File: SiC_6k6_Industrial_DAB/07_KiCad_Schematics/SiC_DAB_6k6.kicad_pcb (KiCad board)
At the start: 6 copper layers, 340 x 250 mm, 259 parts, among them J1 HV+, J10 BoosterPack J1/J3, J11 BoosterPack J2/J4, J12 BoosterPack PWM, J13 +24V IN, J14 CAN, J15 UART, J16 RELAY/FAN, J17 INTERLOCK IN, J18 NTC1, J19 NTC2, J2 HV-, J20 PE, J3 SW_A, J4 SW_B, J5 LV+, J6 LV-, J7 SW_C, J8 SW_D, J9 L1 (via CT), Q1 C3M0032120K, Q2 C3M0032120K, Q3 C3M0032120K, Q4 C3M0032120K, Q5 C3M0016120K, Q6 C3M0016120K, Q7 C3M0016120K, Q8 C3M0016120K, U1 UCC21520DW, U10 LM393, U11 LM393, U12 74HC32, U13 TSR 3-24120, U14 TSR 1-2450, U15 AMS1117-3.3, U16 TCAN332, U17 ULN2003A, U18 PC817, U19 PC817, U2 UCC21520DW, U3 UCC21520DW, U4 UCC21520DW, U5 AMC1301, U6 AMC1301, U7 AMC1301, U8 TLV9062, U9 TLV9062

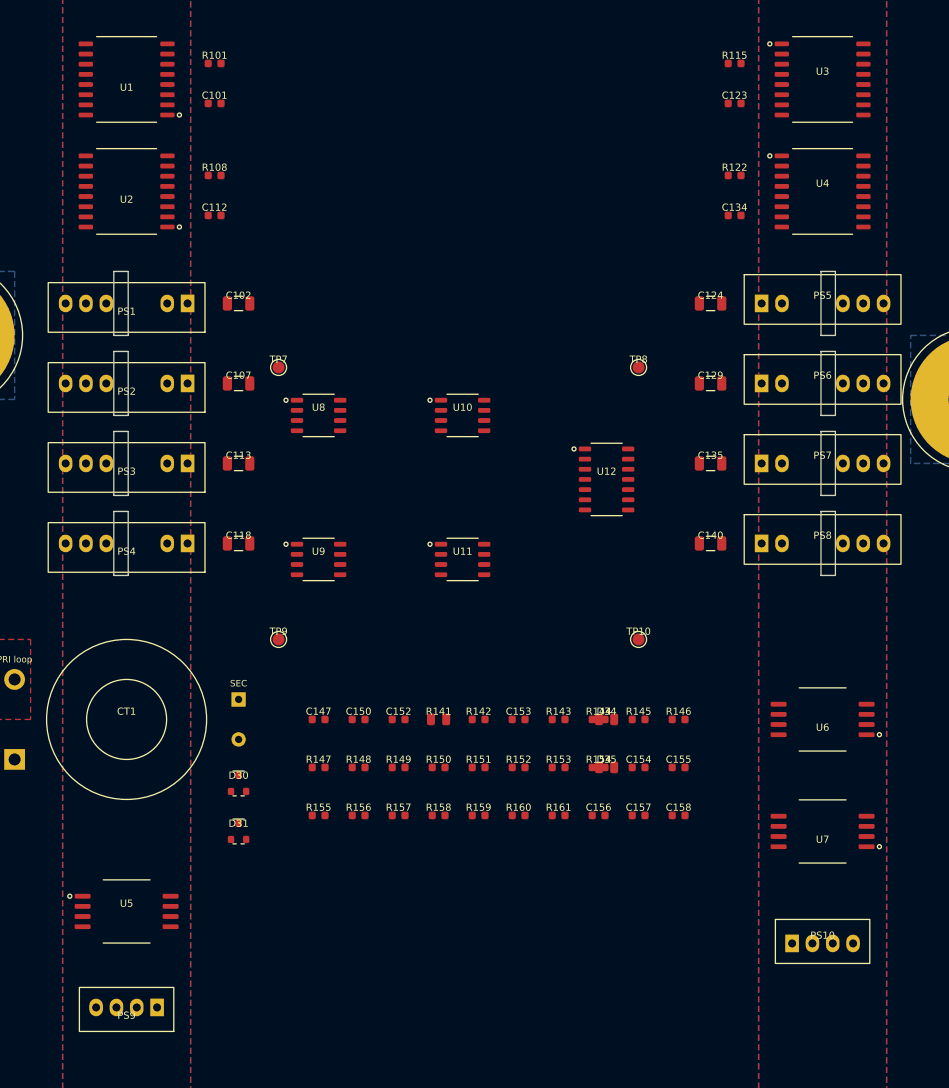
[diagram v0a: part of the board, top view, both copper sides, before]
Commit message: Router hard pass with rip-up retry, exact halo radii, via cost dilation; DAB: driver passives off the fan-out corridors, PS9/PS10 SIP-7 1 W module footprint, 0.5 mm control-power tracks; PSFB: DT resistor/TP placement
- NegotiatedRouter: full/small halo masks give the exact d < hw_a+hw_b+clearance
  overlap test; A* via placement sees the via halo; nets still in conflict after
  the negotiation are re-routed against hard obstacles, with a bounded rip-up
  retry, so emitted copper never violates the clearance model.
- Fan-out: plane-net vias 1.2 mm beyond the long stubs; corridors long+1.5 mm;
  unreachable terminals are reported.
- plot_board.py: matplotlib region renderer for layout review.
- DAB: PS9/PS10 changed from a 2.54 mm SIP-4 (cannot meet the 5.5 mm module
  creepage rule) to a SIP-7 outline 1 W module (part TBD, flagged in BOM and
  insulation table); DT resistors / VCCI caps moved clear of the driver
  fan-out corridors; private regions and slots for PS9/PS10.

Co-Authored-By: Claude Fable 5.1 <noreply@anthropic.com>
Claude-Session: https://claude.ai/code/session_01TJ4PYx4qhHYB2ApeFHUZoW
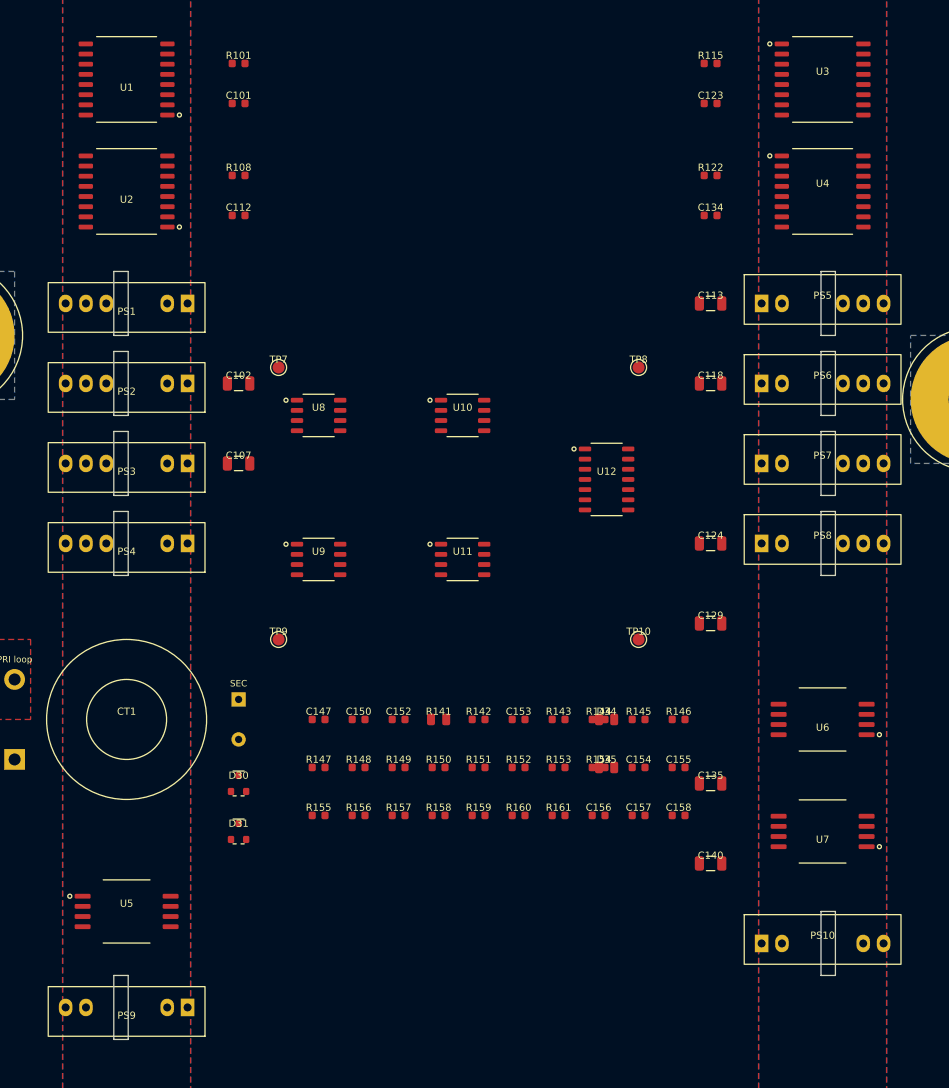
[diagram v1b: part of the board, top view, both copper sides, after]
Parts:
- PS10, PS9: value R1SE-0505 -> ISO 5V/5V 1W SIP-7; footprint SIP-4_IsoDCDC -> SIP-7_IsoDCDC_1W
- moved C113 62.3 mm to (199.0, 48.0)
- moved C118 62.3 mm to (199.0, 58.0)
- moved C135 40.0 mm to (199.0, 108.0)
- moved C140 40.0 mm to (199.0, 118.0)
- moved C124 30.0 mm to (199.0, 78.0)
- moved C129 30.0 mm to (199.0, 88.0)
- moved C102 10.0 mm to (140.0, 58.0)
- moved C107 10.0 mm to (140.0, 68.0)
- moved C101 3.00 mm to (140.0, 23.0)
- moved C112 3.00 mm to (140.0, 37.0)
- moved C123 3.00 mm to (199.0, 23.0)
- moved C134 3.00 mm to (199.0, 37.0)
- moved R101 3.00 mm to (140.0, 18.0)
- moved R108 3.00 mm to (140.0, 32.0)
- moved R115 3.00 mm to (199.0, 18.0)
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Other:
- outline, holes or cut-outs redrawn

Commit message: Router: recursive rip-up retry with state snapshots, same-net task merge; DAB: per-region PE lugs with PE clearance class, net-class fixes (SW_A_CT, SH_N, SH_NS), placement fixes (U15, U18/U19, TP1, bias caps); tools/kicad README
Co-Authored-By: Claude Fable 5.1 <noreply@anthropic.com>
Claude-Session: https://claude.ai/code/session_01TJ4PYx4qhHYB2ApeFHUZoW
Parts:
- added J21: PE_HV, Lug_M5, F.Cu at (42.0, 236.0)
- added J22: PE_LV, Lug_M5, F.Cu at (270.0, 236.0)
- moved C113 64.2 mm to (138.0, 68.0)
- moved C118 64.2 mm to (138.0, 78.0)
- moved C124 20.0 mm to (199.0, 58.0)
- moved C129 20.0 mm to (199.0, 68.0)
- moved C135 20.0 mm to (199.0, 88.0)
- moved C140 20.0 mm to (199.0, 98.0)
- moved C102 10.2 mm to (138.0, 48.0)
- moved C107 10.2 mm to (138.0, 58.0)
- moved TP1 8.94 mm to (96.0, 110.0)
- moved U18 7.00 mm to (150.0, 181.0)
- moved U19 7.00 mm to (162.0, 181.0)
- moved U15 6.00 mm to (182.0, 212.0)
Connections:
- CY1 pad 2: PE -> PE_HV
- CY2 pad 2: PE -> PE_HV
- CY3 pad 2: PE -> PE_LV
- CY4 pad 2: PE -> PE_LV

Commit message: DAB board: intermediate generated board, DRC report and manufacturing outputs (final routing run in progress)
Co-Authored-By: Claude Fable 5.1 <noreply@anthropic.com>
Claude-Session: https://claude.ai/code/session_01TJ4PYx4qhHYB2ApeFHUZoW
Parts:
- C1, C2, C3, C4: footprint C_Film_P52.5 -> SiC_DAB:C_Film_P52.5
- C10, C11, C12, C9: footprint C_Film_P37.5 -> SiC_DAB:C_Film_P37.5
- C101, C104, C106, C109, C111, C112, C115, C117, C120, C122, C123, C126, C128, C131, C133, C134, C137, C139, C142, C144, C145, C146, C147, C148, C149, C150, C151, C152, C153, C154, C155, C156, C157, C158, C165, C166: footprint C_0603 -> SiC_DAB:C_0603
- C102, C103, C107, C108, C113, C114, C118, C119, C124, C125, C129, C130, C135, C136, C140, C141, C161, C163, C164: footprint C_1206 -> SiC_DAB:C_1206
- C105, C110, C116, C121, C127, C132, C138, C143: footprint C_0805 -> SiC_DAB:C_0805
- C13, C14, C15, C16, C5, C6, C7, C8: footprint C_2220 -> SiC_DAB:C_2220
- C159, C160, C162: footprint C_Radial_D8_P3.5 -> SiC_DAB:C_Radial_D8_P3.5
- CT1: footprint CT_Toroid_Straddle -> SiC_DAB:CT_Toroid_Straddle
- CY1, CY2, CY3, CY4: footprint C_Y1_P12.5 -> SiC_DAB:C_Y1_P12.5
- D21, D22, D23, D24, D25, D26, D27, D28, D32, D33: footprint D_SMA -> SiC_DAB:D_SMA
- D30, D31: footprint SOT-23 -> SiC_DAB:SOT-23
- D34, D35: footprint LED_0805 -> SiC_DAB:LED_0805
- F1, F2: footprint Fuse_Terminal_M6 -> SiC_DAB:Fuse_Terminal_M6
- H1, H2, H3, H4, H5, H6: footprint MountingHole_M4 -> SiC_DAB:MountingHole_M4
- J1, J2, J3, J4, J5, J6, J7, J8, J9: footprint Stud_M6 -> SiC_DAB:Stud_M6
- J10, J11: footprint PinHeader_2x10_P2.54 -> SiC_DAB:PinHeader_2x10_P2.54
- J12, J16, J17: footprint PinHeader_1x08_P2.54 -> SiC_DAB:PinHeader_1x08_P2.54
- J13, J14: footprint TerminalBlock_1x02_P5.08 -> SiC_DAB:TerminalBlock_1x02_P5.08
- J15, J18, J19: footprint PinHeader_1x02_P2.54 -> SiC_DAB:PinHeader_1x02_P2.54
- J20, J21, J22: footprint Lug_M5 -> SiC_DAB:Lug_M5
- PS1, PS2, PS3, PS4, PS5, PS6, PS7, PS8: footprint SIP-7_IsoDCDC -> SiC_DAB:SIP-7_IsoDCDC
- PS10, PS9: footprint SIP-7_IsoDCDC_1W -> SiC_DAB:SIP-7_IsoDCDC_1W
- Q1, Q2, Q3, Q4, Q5, Q6, Q7, Q8: footprint TO-247-4_Vertical -> SiC_DAB:TO-247-4_Vertical
- R1, R2, R3, R4, R5, R6: footprint R_2512 -> SiC_DAB:R_2512
- R101, R104, R107, R108, R111, R114, R115, R118, R121, R122, R125, R128, R131, R132, R136, R137, R139, R140, R142, R143, R144, R145, R146, R147, R148, R149, R150, R151, R152, R153, R154, R155, R156, R157, R158, R159, R160, R161, R162, R163, R164, R165, R166, R168, R170, R171, R172: footprint R_0603 -> SiC_DAB:R_0603
- R102, R103, R105, R106, R109, R110, R112, R113, R116, R117, R119, R120, R123, R124, R126, R127, R129, R130, R134, R135, R173: footprint R_1206 -> SiC_DAB:R_1206
- R133, R138, R141, R167, R169: footprint R_0805 -> SiC_DAB:R_0805
- R7: footprint R_Shunt_8518 -> SiC_DAB:R_Shunt_8518
- TP1, TP10, TP11, TP12, TP13, TP2, TP3, TP4, TP5, TP6, TP7, TP8, TP9: footprint TestPoint -> SiC_DAB:TestPoint
- U1, U2, U3, U4: footprint SOIC-16W -> SiC_DAB:SOIC-16W
- U10, U11, U16, U8, U9: footprint SOIC-8 -> SiC_DAB:SOIC-8
- U12: footprint SOIC-14 -> SiC_DAB:SOIC-14
- U13, U14: footprint SIP-3_TSR -> SiC_DAB:SIP-3_TSR
- U15: footprint SOT-223 -> SiC_DAB:SOT-223
- U17: footprint SOIC-16 -> SiC_DAB:SOIC-16
- U18, U19: footprint DIP-4 -> SiC_DAB:DIP-4
- U5, U6, U7: footprint SOIC-8W -> SiC_DAB:SOIC-8W
- moved J21 114.5 mm to (14.0, 125.0)
- moved C159 106.1 mm to (152.0, 90.0)
- moved C162 106.0 mm to (170.0, 90.0)
- moved C160 106.0 mm to (161.0, 90.0)
- moved C135 60.0 mm to (139.0, 88.0)
- moved C140 60.0 mm to (139.0, 98.0)
- moved D34 50.2 mm to (140.0, 120.0)
- moved D35 50.2 mm to (140.0, 126.0)
- moved C166 35.5 mm to (181.0, 196.0)
- moved R165 35.5 mm to (186.0, 196.0)
- moved R166 35.5 mm to (191.0, 196.0)
- moved C163 15.0 mm to (161.0, 196.0)
- moved C164 15.0 mm to (166.0, 196.0)
- moved C165 15.0 mm to (171.0, 196.0)
- moved R164 15.0 mm to (176.0, 196.0)
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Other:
- outline, holes or cut-outs redrawn

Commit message: DAB board: intermediate generated board and DRC report (run 17: 29 errors, routing run 19 in progress)
Co-Authored-By: Claude Fable 5.1 <noreply@anthropic.com>
Claude-Session: https://claude.ai/code/session_01TJ4PYx4qhHYB2ApeFHUZoW
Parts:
- moved TP6 23.9 mm to (232.0, 80.0)
- moved J20 12.0 mm to (152.0, 242.0)
- moved C135 11.7 mm to (145.0, 98.0)
- moved J3 8.00 mm to (92.0, 105.0)
- moved TP1 8.00 mm to (96.0, 118.0)
- moved TP10 6.08 mm to (199.0, 84.0)
- moved C140 6.00 mm to (145.0, 98.0)
- moved D30 6.00 mm to (146.0, 108.0)
- moved D31 6.00 mm to (146.0, 114.0)
- moved J7 4.00 mm to (236.0, 60.0)
- moved TP3 4.00 mm to (30.0, 56.0)
- moved U17 4.00 mm to (176.0, 186.0)
- moved C159 2.00 mm to (150.0, 90.0)
- moved C160 1.00 mm to (160.0, 90.0)

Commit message: DAB board: intermediate generated board and DRC report (run 19: 18 errors; run 20 in progress)
Co-Authored-By: Claude Fable 5.1 <noreply@anthropic.com>
Claude-Session: https://claude.ai/code/session_01TJ4PYx4qhHYB2ApeFHUZoW
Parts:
- moved J3 32.0 mm to (93.0, 73.0)
- moved TP1 32.0 mm to (96.0, 86.0)
- moved TP9 6.32 mm to (143.0, 84.0)
- moved C140 6.00 mm to (145.0, 104.0)
- moved C13 4.00 mm to (248.0, 38.0)
- moved C14 4.00 mm to (266.0, 38.0)
- moved C15 4.00 mm to (294.0, 38.0)
- moved C16 4.00 mm to (312.0, 38.0)
- moved C8 4.00 mm to (96.0, 38.0)
- moved J20 2.00 mm to (150.0, 242.0)

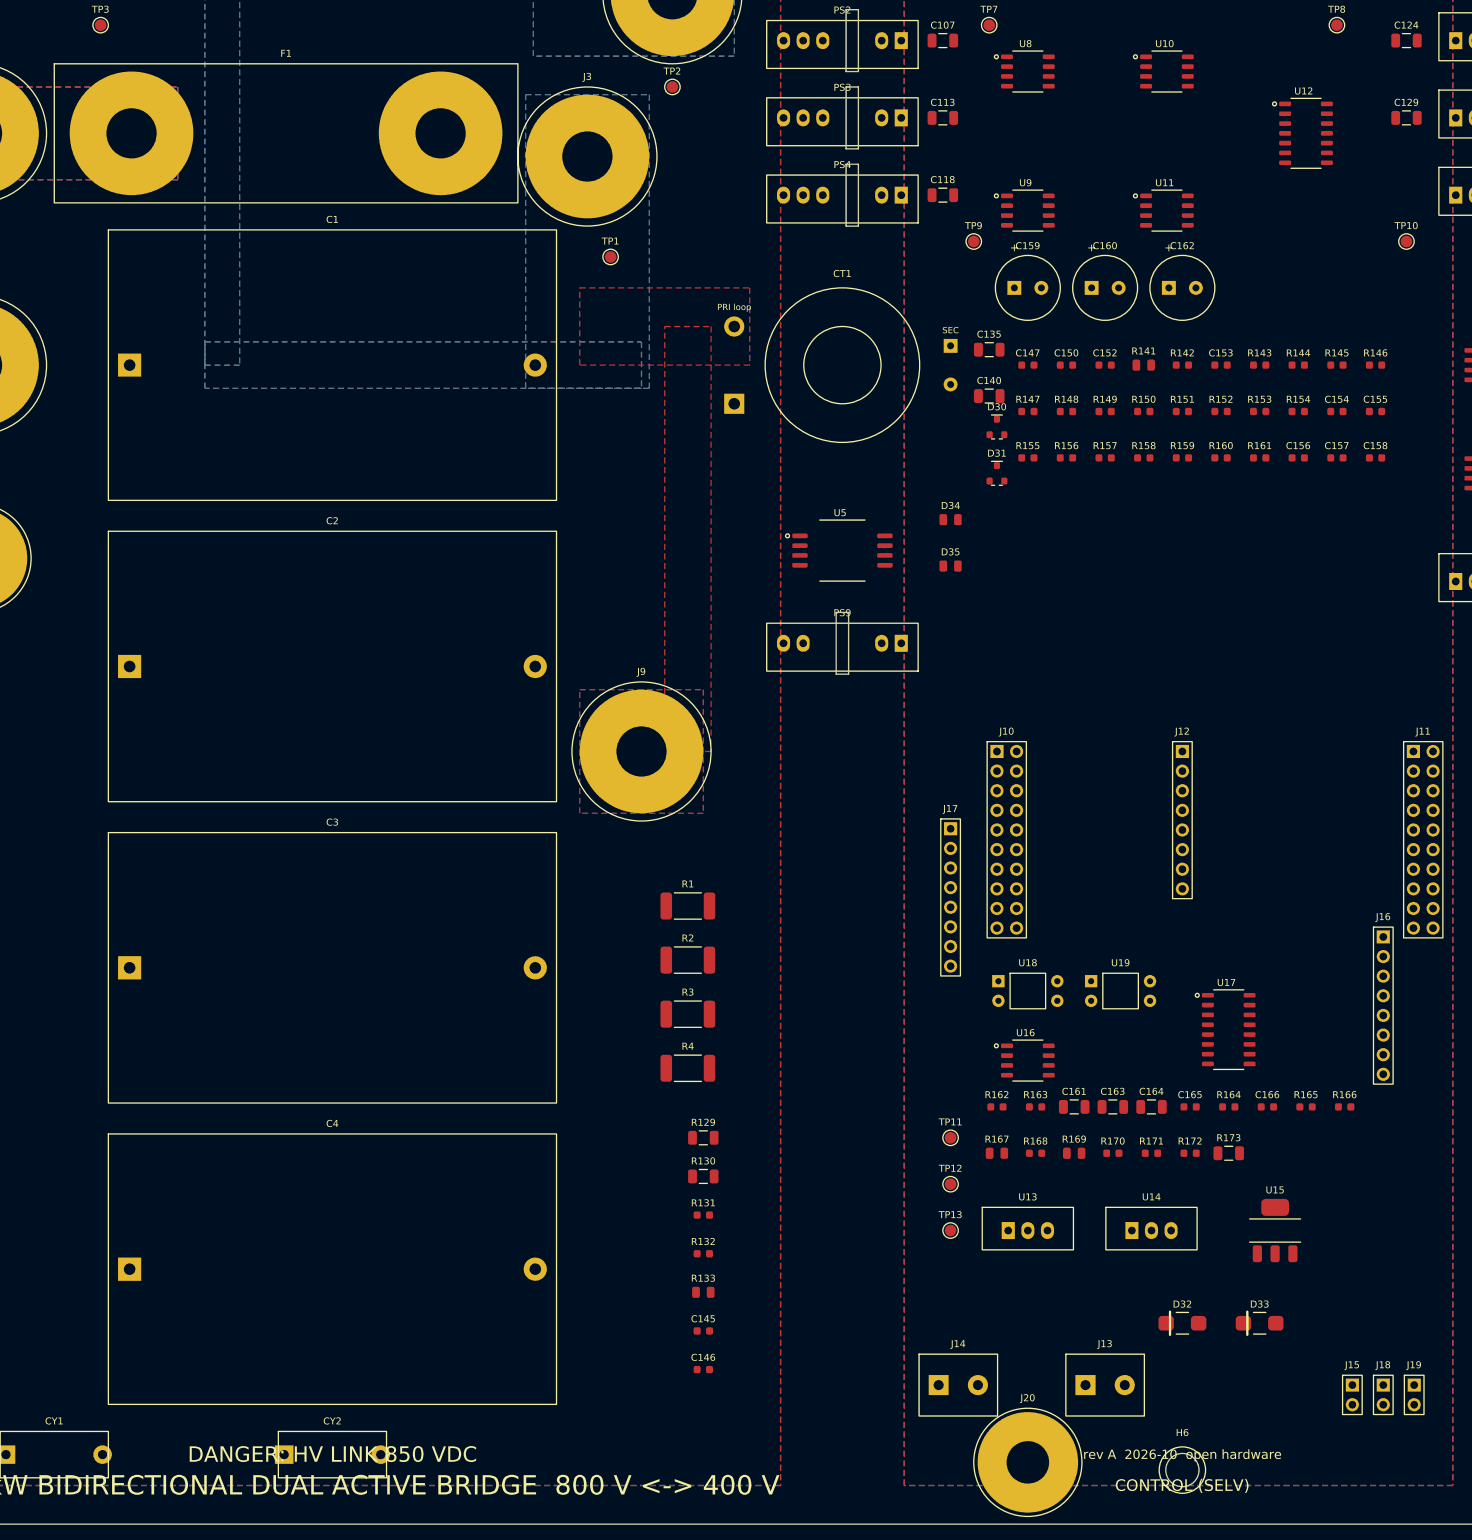
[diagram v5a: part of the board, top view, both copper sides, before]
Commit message: DAB board: intermediate generated board and DRC report (run 20: 6 errors; run 21 in progress)
Co-Authored-By: Claude Fable 5.1 <noreply@anthropic.com>
Claude-Session: https://claude.ai/code/session_01TJ4PYx4qhHYB2ApeFHUZoW
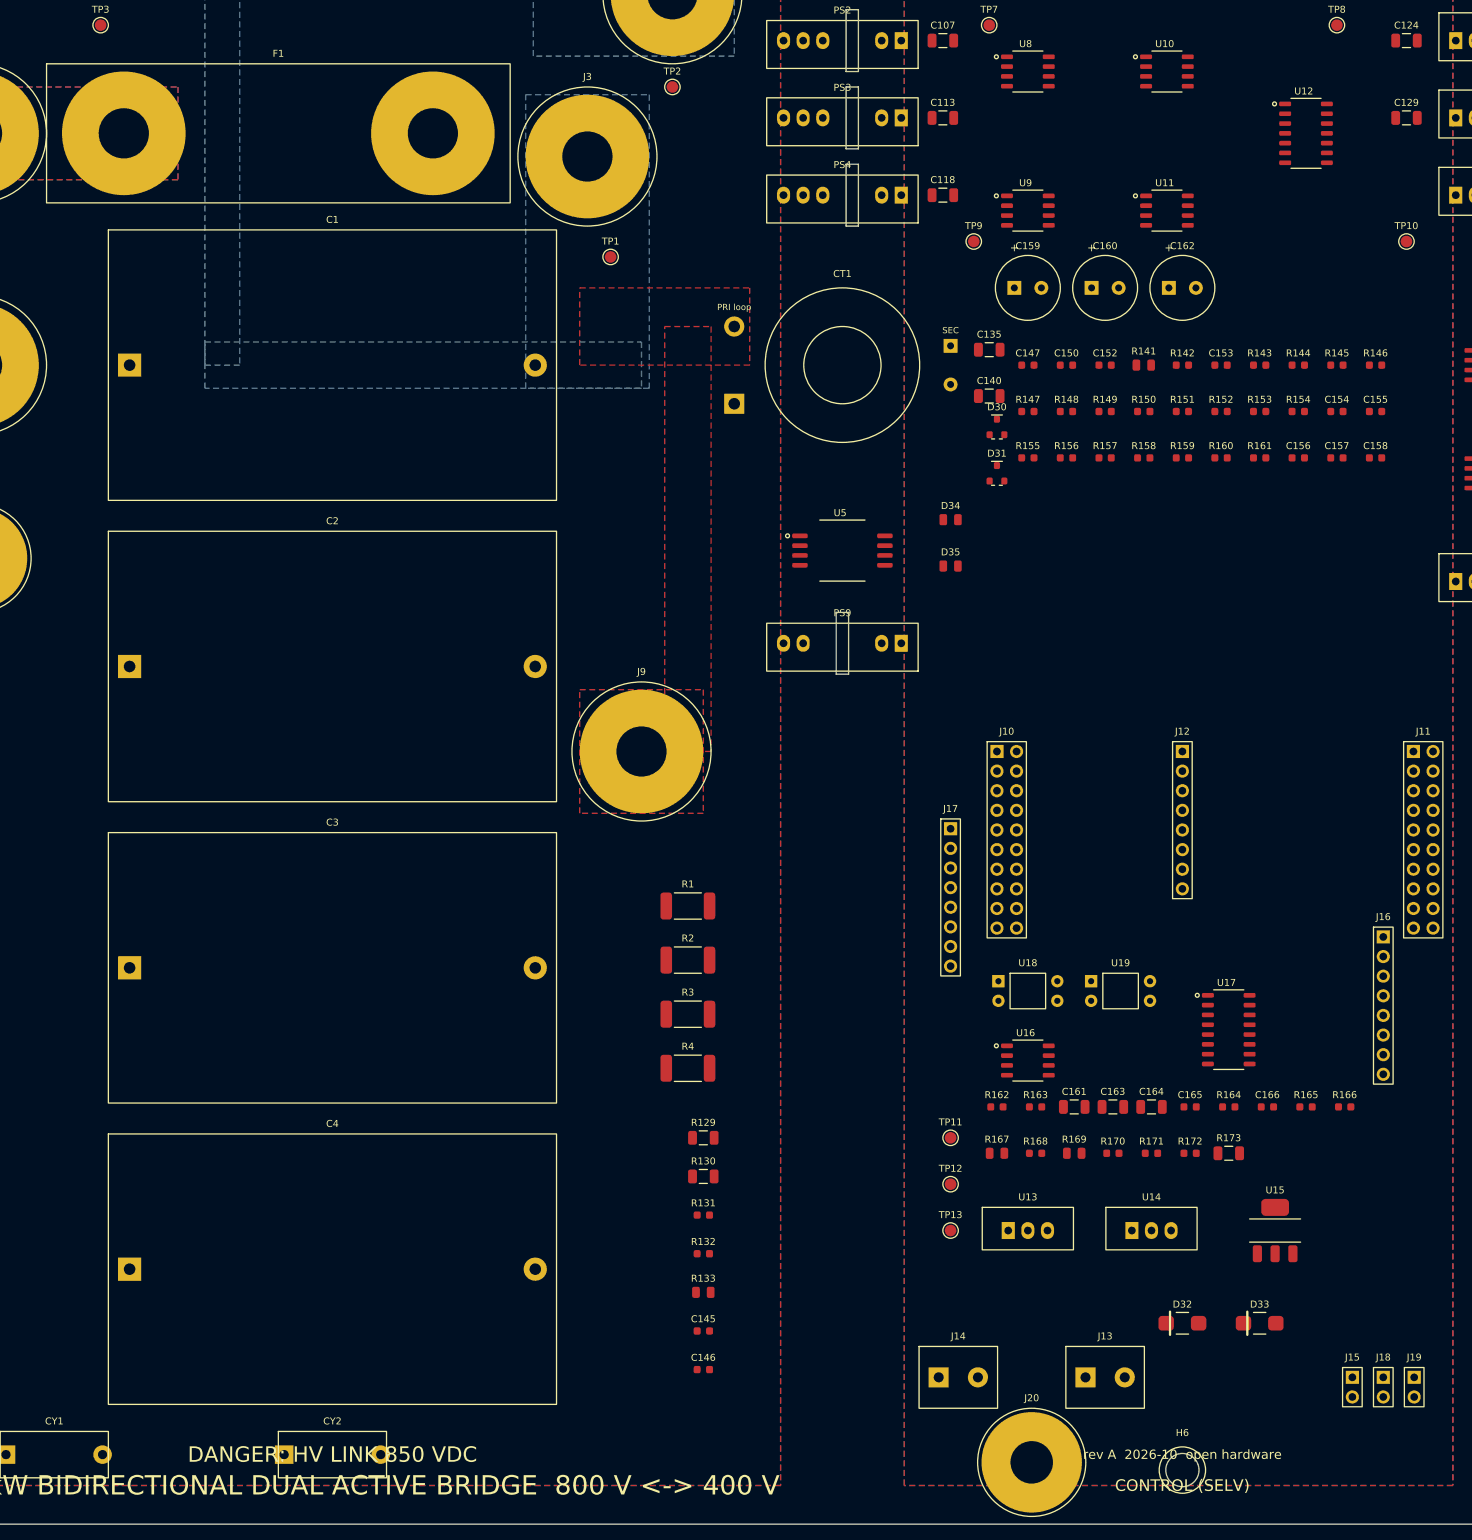
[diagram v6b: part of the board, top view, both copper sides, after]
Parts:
- moved F1 1.00 mm to (53.0, 70.0)
- moved J13 1.00 mm to (160.0, 231.0)
- moved J14 1.00 mm to (141.0, 231.0)
- moved J15 1.00 mm to (192.0, 231.0)
- moved J18 1.00 mm to (196.0, 231.0)
- moved J19 1.00 mm to (200.0, 231.0)
- moved J20 0.50 mm to (150.5, 242.0)
